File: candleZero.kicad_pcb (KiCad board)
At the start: 2 copper layers, 14 x 20.5 mm, 25 parts, among them J1 CONN_02X02, J5 CONN_02X05, J6 DB9_MALE, U1 STM32F072C8Ux, U2 TLV70233DBV, U3 TJA1051TK/3

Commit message: v0.2
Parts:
- added J2: TEST_1P, pins:Pin_Header_Straight_1x01_Pitch2.00mm, F.Cu at (161.8, 101.2)
- added J3: TEST_1P, pins:Pin_Header_Straight_1x01_Pitch2.00mm, F.Cu at (153.2, 101.2)
- added J4: TEST_1P, pins:Pin_Header_Straight_1x01_Pitch2.00mm, F.Cu at (151.5, 100.0)
- J1: value CONN_02X02 -> TEST_1P; footprint Pin_Headers:Pin_Header_Straight_2x02_Pitch1.27mm -> pins:Pin_Header_Straight_1x01_Pitch2.00mm
- J6: footprint Connectors:DB9M_CI -> subd9-small:DB9M_CI_SMALL
- moved J1 10.1 mm to (163.5, 100.0), turned to 270 degrees
- moved R5 5.00 mm to (156.0, 94.0)
- moved R6 5.00 mm to (154.5, 94.0)
- moved C2 4.61 mm to (159.0, 97.0)
- moved C1 4.27 mm to (153.0, 94.0), turned to 270 degrees
- moved C5 4.12 mm to (163.0, 94.0)
- moved R7 2.92 mm to (153.0, 91.0), turned to 90 degrees
- moved J6 2.54 mm to (157.5, 88.0)
- moved J5 2.04 mm to (155.0, 101.5)
- moved C8 1.58 mm to (159.0, 94.0)
- moved R3 1.58 mm to (157.5, 94.0)
- moved C4 1.35 mm to (163.2, 97.5)
- moved C7 1.35 mm to (161.2, 97.5)
- moved R4 0.75 mm to (162.0, 90.2)
- moved C6 0.71 mm to (161.5, 94.0)
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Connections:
- net Net-(J6-Pad2) renamed /CAN_L
- net Net-(J6-Pad7) renamed /CAN_H
- J5 pad 7: Net-(J5-Pad7) -> GND
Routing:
- net +5V: track 25.7 -> 10.4 mm
- net GND: track 35.7 -> 27.9 mm, vias 8 -> 6
- net Net-(D3-Pad2): track 7.04 -> 1.35 mm
- net Net-(R1-Pad2): track 11.6 -> 7.68 mm
- net +3V3: track 14.5 -> 17.9 mm
- net USB_DP: track 2.99 -> 6.16 mm, vias 0 -> 1
- net Net-(D1-Pad2): track 2.22 -> 5.12 mm
- net Net-(D2-Pad2): track 1.92 -> 4.41 mm
- net (no net): track 2.34 -> 0.00 mm
- net SWCLK: track 2.78 -> 4.54 mm, vias 0 -> 1
- net SWDIO: track 1.83 -> 3.42 mm
- net /CAN_L: track 8.31 -> 9.39 mm
- net /CAN_H: track 7.57 -> 6.50 mm
- net USB_DM: track 3.70 -> 4.73 mm
- net CAN_S: track 7.60 -> 8.28 mm
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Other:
- board size 14 x 20.5 mm -> 15 x 17 mm
- net class 3V3 added: clearance 0.1524, trace_width 0.254, via_dia 0.635, via_drill 0.381
- net class 5V added: clearance 0.1524, trace_width 0.254, via_dia 0.635, via_drill 0.381
- net class CAN added: clearance 0.1524, trace_width 0.254, via_dia 0.635, via_drill 0.381
- net class Default: trace_width 0.2032 -> 0.1524
- rule trace_min: 0.127 -> 0.1524
- board text added: "candleZero bytewerk.org"
- board text added: "v0.2"
- board text removed: "PWR"
- board text removed: "RX"
- board text removed: "TX"
- board text removed: "candleZero v0.1"
- board text removed: "https://bytewerk.org/"

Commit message: v0.3
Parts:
- removed D2, D3: LED, LEDs:LED_0603
- removed R1: dnp, Resistors_SMD:R_0603
- D1: value LED -> LED_RGB; footprint LEDs:LED_0603 -> LEDs:LED_RGB_PLCC-6; moved to B.Cu
- J5: footprint Pin_Headers:Pin_Header_Straight_2x05_Pitch1.27mm -> jtag:Pin_Header_Straight_2x05_Pitch1.27mm
- R4: moved to B.Cu
- moved C9 9.27 mm to (160.5, 91.5)
- moved R7 7.91 mm to (157.5, 97.5)
- moved C2 6.31 mm to (153.0, 95.0), turned to 270 degrees
- moved R2 5.25 mm to (160.5, 94.3), turned to 90 degrees
- moved C3 4.53 mm to (153.0, 97.5)
- moved R5 3.81 mm to (154.5, 97.5)
- moved R6 3.81 mm to (156.0, 97.5)
- moved C8 3.50 mm to (159.0, 97.5), turned to 90 degrees
- moved R3 3.18 mm to (154.5, 95.0)
- moved D1 3.01 mm to (157.5, 93.0), turned to 270 degrees
- moved C5 2.55 mm to (163.5, 91.5)
- moved C1 2.50 mm to (153.0, 91.5)
- moved J3 2.15 mm to (151.5, 100.0)
- moved J4 2.15 mm to (153.2, 101.2)
- moved C6 2.02 mm to (163.5, 94.2)
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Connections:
- net Net-(R1-Pad2) renamed /BOOT
- D1 pad 1: GND -> LED_R
- D1 pad 2: Net-(D1-Pad2) -> LED_G
- R5 pad 2: Net-(D1-Pad2) -> Net-(D1-Pad6)
- R6 pad 2: Net-(D2-Pad2) -> Net-(D1-Pad5)
- R7 pad 2: Net-(D3-Pad2) -> Net-(D1-Pad4)
- U1 pad 10: LED1 -> Net-(U1-Pad10)
- U1 pad 11: LED2 -> Net-(U1-Pad11)
- U1 pad 12: Net-(U1-Pad12) -> LED_R
- U1 pad 13: Net-(U1-Pad13) -> LED_G
- U1 pad 15: Net-(U1-Pad15) -> LED_B
- U1 pad 18: Net-(U1-Pad18) -> GND
- U1 pad 19: Net-(U1-Pad19) -> GND
- U1 pad 20: Net-(U1-Pad20) -> GND
- U1 pad 21: Net-(U1-Pad21) -> GND
- U1 pad 22: Net-(U1-Pad22) -> GND
- U1 pad 25: Net-(U1-Pad25) -> GND
- U1 pad 26: Net-(U1-Pad26) -> GND
- U1 pad 27: Net-(U1-Pad27) -> GND
- U1 pad 28: Net-(U1-Pad28) -> GND
- U1 pad 29: Net-(U1-Pad29) -> GND
- U1 pad 30: Net-(U1-Pad30) -> GND
- U1 pad 31: Net-(U1-Pad31) -> GND
- U1 pad 38: Net-(U1-Pad38) -> GND
- U1 pad 39: Net-(U1-Pad39) -> GND
- U1 pad 40: Net-(U1-Pad40) -> GND
- U1 pad 41: Net-(U1-Pad41) -> GND
- U1 pad 42: Net-(U1-Pad42) -> GND
- U1 pad 43: Net-(U1-Pad43) -> GND
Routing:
- net GND: track 27.9 -> 66.1 mm, vias 6 -> 8
- net LED_B: track 0.00 -> 9.01 mm, vias 0 -> 1
- net NRST: track 16.1 -> 24.1 mm
- net LED_G: track 0.00 -> 7.97 mm, vias 0 -> 1
- net /BOOT: track 7.68 -> 1.98 mm
- net CAN_S: track 8.28 -> 13.4 mm
- net Net-(D1-Pad2): track 5.12 -> 0.00 mm, vias 1 -> 0
- net LED_R: track 0.00 -> 4.87 mm, vias 0 -> 1
- net Net-(D2-Pad2): track 4.41 -> 0.00 mm, vias 1 -> 0
- net Net-(D1-Pad6): track 0.00 -> 3.55 mm
- net Net-(D1-Pad5): track 0.00 -> 3.42 mm
- net /CAN_L: track 9.39 -> 6.18 mm, vias 0 -> 1
- net LED2: track 2.90 -> 0.00 mm
- net Net-(D1-Pad4): track 0.00 -> 2.66 mm
- net /CAN_H: track 6.50 -> 8.52 mm
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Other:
- board size 15 x 17 mm -> 15 x 16 mm
- net class CAN: trace_width 0.254 -> 0.1524; via_dia 0.635 -> 0.508; via_drill 0.381 -> 0.254
- board text added: "bytewerk.org"
- board text added: "candleZero"
- board text added: "v0.3"
- board text removed: "candleZero bytewerk.org"
- board text removed: "v0.2"

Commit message: v0.4
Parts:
- J6: moved to B.Cu
- moved C2 0.30 mm to (153.0, 94.8)
- moved R3 0.30 mm to (154.5, 94.8)
- turned J6 to 180 degrees
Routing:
- net /CAN_L: track 6.18 -> 12.2 mm, vias 1 -> 2
- net /CAN_H: track 8.52 -> 10.7 mm, vias 1 -> 2
- net CAN_S: track 13.4 -> 12.3 mm
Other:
- board text added: "v0.4"
- board text removed: "v0.3"

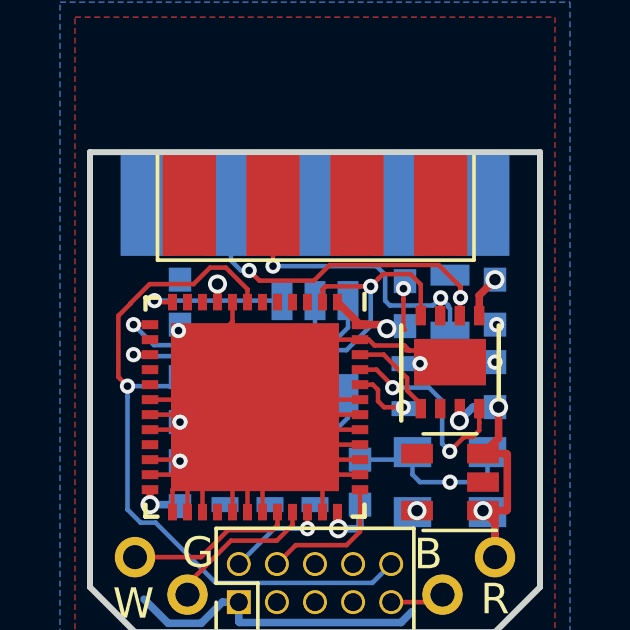
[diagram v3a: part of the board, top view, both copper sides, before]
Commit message: fix led colors
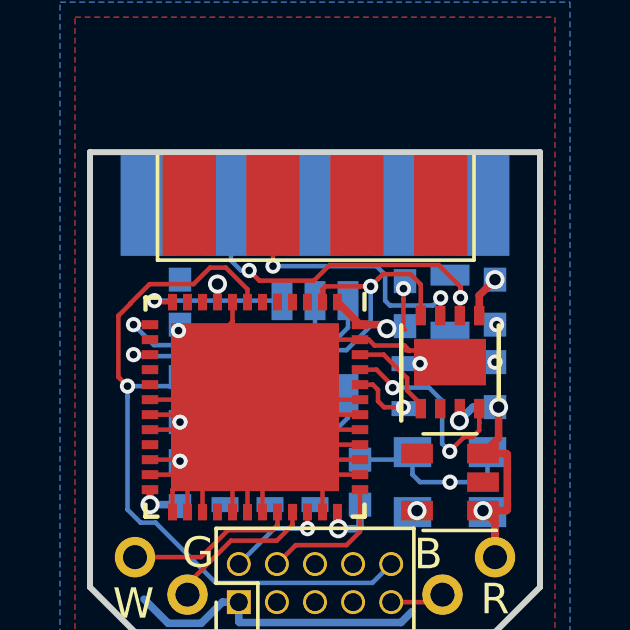
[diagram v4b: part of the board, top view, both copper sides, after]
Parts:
- R5, R6: value R -> 10R
- R7: value R -> 120R
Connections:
- D1 pad 1: LED_R -> LED_B
- D1 pad 3: LED_B -> LED_R
- U1 pad 12: LED_R -> LED_B
- U1 pad 15: LED_B -> LED_R
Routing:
- net LED_R: track 4.87 -> 9.01 mm
- net LED_B: track 9.01 -> 4.87 mm

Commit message: v0.5 / bga design test
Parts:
- removed J2, J3, J4: TEST_1P, pins:Pin_Header_Straight_1x01_Pitch2.00mm
- removed J5: CONN_02X05, jtag:Pin_Header_Straight_2x05_Pitch1.27mm
- removed J6: DB9_MALE, subd9-small:DB9M_CI_SMALL
- removed R4: dnp, Resistors_SMD:R_0805
- removed R7: 120R, Resistors_SMD:R_0603
- added C10: 100nF, Capacitor_SMD:C_0603_1608Metric, B.Cu at (148.8, 73.2)
- added C11: 1uF, Capacitor_SMD:C_0603_1608Metric, B.Cu at (153.2, 79.1)
- added R1: R, Resistor_SMD:R_0603_1608Metric, B.Cu at (153.2, 74.5)
- added TP1: D-, TestPoint:TestPoint_THTPad_1.5x1.5mm_Drill0.7mm, F.Cu at (142.5, 81.5)
- added TP2: D+, TestPoint:TestPoint_THTPad_1.5x1.5mm_Drill0.7mm, F.Cu at (146.4, 81.5)
- added TP3: +5V, TestPoint:TestPoint_THTPad_1.5x1.5mm_Drill0.7mm, F.Cu at (150.5, 81.5)
- added TP4: GND, TestPoint:TestPoint_THTPad_1.5x1.5mm_Drill0.7mm, F.Cu at (154.7, 81.5)
- added TP5: VCC, TestPoint:TestPoint_Pad_D1.0mm, F.Cu at (148.5, 81.0)
- added TP6: RESET, TestPoint:TestPoint_Pad_D1.0mm, F.Cu at (143.9, 79.4)
- added TP7: SWDIO, TestPoint:TestPoint_Pad_D1.0mm, F.Cu at (147.4, 79.4)
- added TP8: SWCLK, TestPoint:TestPoint_Pad_D1.0mm, F.Cu at (149.0, 79.4)
- added TP9: GND, TestPoint:TestPoint_Pad_D1.0mm, F.Cu at (142.3, 79.4)
- C1, C2, C3, C5, C6, C8: footprint Capacitors_SMD:C_0603 -> Capacitor_SMD:C_0603_1608Metric
- C4: value 10uF/10V -> 100nF; footprint Capacitors_SMD:C_0805 -> Capacitor_SMD:C_0603_1608Metric; moved to F.Cu
- C7: value 10uF -> 1uF; footprint Capacitors_SMD:C_0805 -> Capacitor_SMD:C_0603_1608Metric; moved to F.Cu
- C9: value 100nF -> 1uF; footprint Capacitors_SMD:C_0603 -> Capacitor_SMD:C_0603_1608Metric; moved to F.Cu
- D1: footprint LEDs:LED_RGB_PLCC-6 -> LED_SMD:LED_RGB_PLCC-6
- J1: value TEST_1P -> DB9_Male; footprint pins:Pin_Header_Straight_1x01_Pitch2.00mm -> Connector_Dsub:DSUB-9_Male_EdgeMount_P2.77mm
- R2, R3: value 10K -> R; footprint Resistors_SMD:R_0603 -> Resistor_SMD:R_0603_1608Metric
- R5, R6: value 10R -> 10k; footprint Resistors_SMD:R_0603 -> Resistor_SMD:R_0603_1608Metric; moved to F.Cu
- U1: value STM32F072C8Ux -> STM32F072RBHx; footprint qfn48:QFN-48_EP_7x7_Pitch0.5mm -> Package_BGA:UFBGA-64_5x5mm_Layout8x8_P0.5mm
- U2: value TLV70233DBV -> TJA1051T-3; footprint TO_SOT_Packages_SMD:SOT-23-5 -> Package_DFN_QFN:DFN-8_2x2mm_P0.5mm
- U3: value TJA1051TK/3 -> TLV70233_SOT23-5; footprint Housings_DFN_QFN:DFN-8-1EP_3x3mm_Pitch0.65mm -> Package_TO_SOT_SMD:SOT-23-5
- moved J1 33.5 mm to (148.6, 70.0), turned to 180 degrees
- moved C6 29.5 mm to (142.8, 73.2), turned to 180 degrees
- moved C8 27.7 mm to (145.8, 73.2), turned to 0 degrees
- moved C4 25.4 mm to (154.2, 73.8), turned to 0 degrees
- moved U2 25.3 mm to (151.5, 74.5), turned to 90 degrees
- moved C5 24.8 mm to (142.8, 77.8), turned to 180 degrees
- moved R6 23.9 mm to (149.5, 74.5), turned to 270 degrees
- moved C3 23.7 mm to (142.8, 76.2), turned to 180 degrees
- moved C2 22.5 mm to (142.8, 74.7), turned to 180 degrees
- moved U1 21.8 mm to (145.2, 75.8)
- moved R5 20.8 mm to (149.5, 77.3)
- moved C7 20.1 mm to (155.0, 78.2)
- moved R2 19.7 mm to (153.2, 76.0), turned to 0 degrees
- moved D1 19.2 mm to (148.6, 76.0), turned to 0 degrees
- moved U3 18.1 mm to (152.3, 78.2), turned to 180 degrees
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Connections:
- C1 pad 1: +3V3 -> RESET
- C2 pad 1: NRST -> +3V3
- C4 pad 1: +5V -> +3V3
- C6 pad 1: +5V -> +3V3
- C7 pad 1: +3V3 -> +5V
- C9 pad 1: +3V3 -> GND
- C9 pad 2: GND -> +5V
- D1 pad 1: LED_B -> R
- D1 pad 2: LED_G -> G
- D1 pad 3: LED_R -> B
- J1 pad 1: +5V -> Net-(J1-Pad1)
- R2 pad 1: /BOOT -> Net-(D1-Pad5)
- R2 pad 2: GND -> +3V3
- R3 pad 1: +3V3 -> Net-(D1-Pad6)
- R3 pad 2: CAN_S -> +3V3
- R5 pad 1: +3V3 -> BOOT0
- R5 pad 2: Net-(D1-Pad6) -> GND
- R6 pad 1: +3V3 -> SILENT
- R6 pad 2: Net-(D1-Pad5) -> +3V3
- U2 pad 1: +5V -> TXD
- U2 pad 4: (no net) -> RXD
- U3 pad 1: CAN_TX -> +5V
- U3 pad 4: CAN_RX -> Net-(U3-Pad4)
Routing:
- net GND: track 66.0 -> 18.9 mm, vias 8 -> 18
- net NRST: track 24.1 -> 0.00 mm, vias 1 -> 0
- net RESET: track 0.00 -> 16.6 mm, vias 0 -> 2
- net CAN_S: track 12.3 -> 0.00 mm, vias 1 -> 0
- net /CAN_L: track 12.2 -> 0.00 mm, vias 2 -> 0
- net /CAN_H: track 10.7 -> 0.00 mm, vias 2 -> 0
- net SILENT: track 0.00 -> 10.6 mm, vias 0 -> 2
- net B: track 0.00 -> 9.98 mm, vias 0 -> 1
- net LED_R: track 9.01 -> 0.00 mm, vias 1 -> 0
- net RXD: track 0.00 -> 8.48 mm, vias 0 -> 2
- net LED_G: track 7.97 -> 0.00 mm, vias 1 -> 0
- net G: track 0.00 -> 7.15 mm, vias 0 -> 1
- net CAN_RX: track 6.99 -> 0.00 mm, vias 2 -> 0
- net +3V3: track 18.2 -> 24.5 mm, vias 6 -> 18
- net D-: track 0.00 -> 6.27 mm
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- added copper zone on In1.Cu, net +3V3
- added copper zone on In2.Cu, net GND
- removed copper zone on B.Cu, net +3V3
- removed copper zone on F.Cu, net GND
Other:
- board size 15 x 16 mm -> 15.4 x 15 mm
- copper layers 2 -> 4
- net class 3V3 removed
- net class 5V removed
- net class CAN removed
- net class Default: clearance 0.1524 -> 0.2; trace_width 0.1524 -> 0.254; via_dia 0.508 -> 0.36
- rule pad_to_mask_clearance: 0.0254 -> 0.0508
- rule trace_clearance: 0.1524 -> 0.2
- rule trace_min: 0.1524 -> 0.127
- rule via_min_size: 0.508 -> 0.36
- board text added: "Zero"
- board text added: "candle"
- board text added: "v0.5"
- board text removed: "candleZero"
- board text removed: "v0.4"
